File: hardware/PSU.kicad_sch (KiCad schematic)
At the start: 30 parts, among them J1 UJ20-C-H-G-SMT-2A-P16-TR, U2 REF35330QDBVR, U4 LM27762, U5 NCP1117-3.3_SOT223

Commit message: feat(hardware): Update switch footprint
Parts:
- TP10, TP11, TP12, TP13, TP14, TP9: Purchase Link (none) -> https://www.digikey.com/en/products/detail/koa-speer-electr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
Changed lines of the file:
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@@
 			)
 		)
+		(property "Purchase Link" "https://www.digikey.com/en/products/detail/koa-speer-electronics-inc/RCUCTE/11476561"
+			(at 191.77 130.81 0)
+			(effects
+				(font
+					(size 1.27 1.27)
+				)
+				(hide yes)
+			)
+		)
 		(pin "1"
 		)
@@
 			)
 		)
+		(property "Purchase Link" "https://www.digikey.com/en/products/detail/koa-speer-electronics-inc/RCUCTE/11476561"
+			(at 242.57 121.92 0)
+			(effects
+				(font
+					(size 1.27 1.27)
+				)
+				(hide yes)
+			)
+		)
 		(pin "1"
 		)
@@
 			)
 		)
+		(property "Purchase Link" "https://www.digikey.com/en/products/detail/koa-speer-electronics-inc/RCUCTE/11476561"
+			(at 248.92 139.7 0)
+			(effects
+				(font
+					(size 1.27 1.27)
+				)
+				(hide yes)
+			)
+		)
 		(pin "1"
 		)
@@
 			)
 		)
+		(property "Purchase Link" "https://www.digikey.com/en/products/detail/koa-speer-electronics-inc/RCUCTE/11476561"
+			(at 218.44 139.7 0)
+			(effects
+				(font
+					(size 1.27 1.27)
+				)
+				(hide yes)
+			)
+		)
 		(pin "1"
 		)
@@
 			)
 		)
+		(property "Purchase Link" "https://www.digikey.com/en/products/detail/koa-speer-electronics-inc/RCUCTE/11476561"
+			(at 233.68 139.7 0)
+			(effects
+				(font
+					(size 1.27 1.27)
+				)
+				(hide yes)
+			)
+		)
 		(pin "1"
 		)
@@
 			(at 224.79 121.92 0)
 			(effects
+				(font
+					(size 1.27 1.27)
+				)
+				(hide yes)
+			)
+		)
+		(property "Purchase Link" "https://www.digikey.com/en/products/detail/koa-speer-electronics-inc/RCUCTE/11476561"
+			(at 224.79 121.92 0)
+			(effects

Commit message: feat(hardware): updted design rules
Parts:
- removed NT1, NT2: NetTie_2, NetTie:NetTie-2_SMD_Pad0.5mm, symbol Device:NetTie_2
- added FB1: FerriteBead, Resistor_SMD:R_0603_1608Metric, symbol Device:FerriteBead
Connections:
- net +3V3: now also FB1.1
- net +3V3A: now also FB1.2

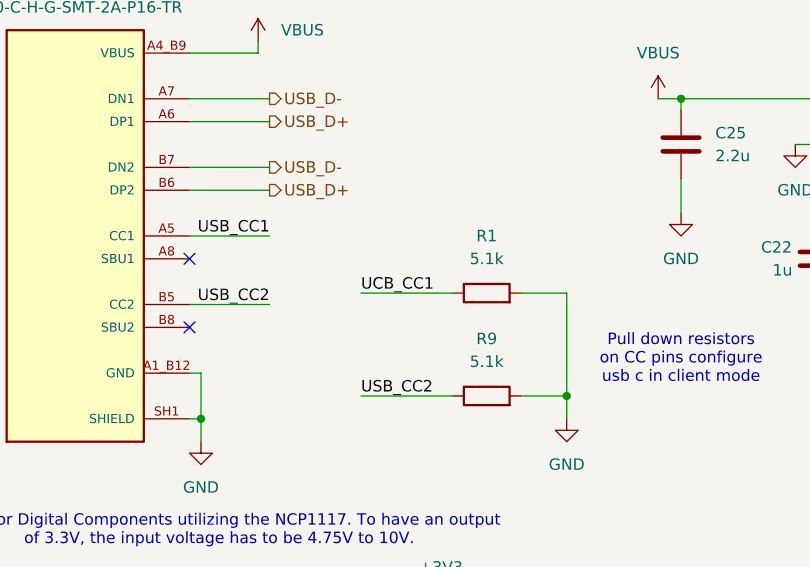
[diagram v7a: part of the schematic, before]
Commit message: feat(hardware): Add VBUS plane
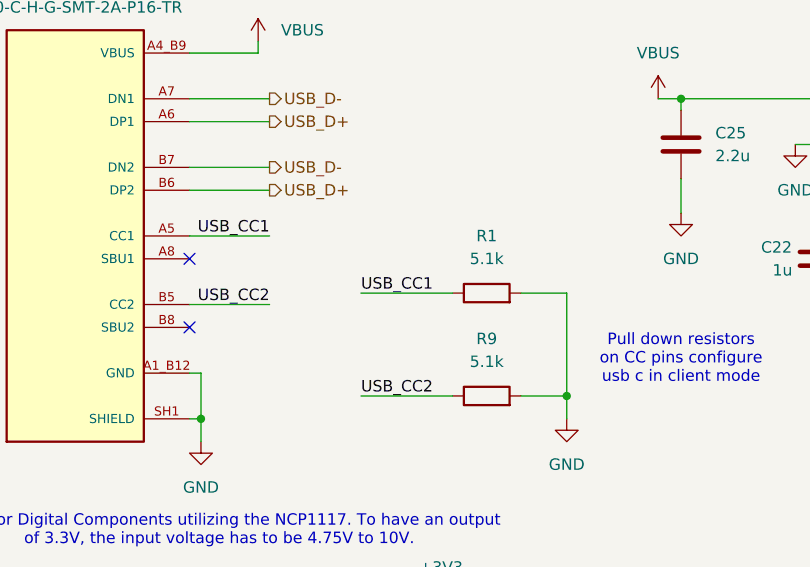
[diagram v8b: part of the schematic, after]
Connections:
- net UCB_CC1 is gone; now on net USB_CC1: R1.1
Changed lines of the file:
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@@
 		)
 	)
-	(label "UCB_CC1"
+	(label "USB_CC1"
 		(at 102.87 74.93 0)
 		(effects
